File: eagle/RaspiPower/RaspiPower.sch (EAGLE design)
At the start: 26 parts, among them J5 AVR_SPI_PROG_3X2PTH, K1 4052

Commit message: Last changes before routing, added power LED
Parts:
- added J10: (no value), SparkFun-Connectors:CONN_01PTH_NO_SILK_YES_STOP
- added JOUT: (no value), SparkFun-Connectors:CONN_02LOCK_LONGPADS
- added LED_POWER2: (no value), SparkFun-LED:LED-FKIT-1206
- added R6: 1k, resistor:R-EU_R1206W
- D1: device diode:DIODE-D-2.5 -> diode:DIODE-D-5
- J6: device SparkFun-Connectors:CONN_02LOCK_LONGPADS -> SparkFun-Connectors:CONN_01PTH_NO_SILK_YES_STOP
- R4, R5: value 1k -> 10k
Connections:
- new net N$1: LED_POWER2.A, R6.1
- net GND: now also JOUT.2, LED_POWER2.C; no longer J6.2
- net N$3: now also JOUT.1; no longer J6.1
- net VCC: now also R6.2
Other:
- note added: "No resistor: - 97ohm in the relay coil for 942H-2C-5DS - 131ohm in the relay coil for HK4100F"
- note removed: "No resistor (97ohm in the relay coil)"
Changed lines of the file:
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@@
 <part name="K1" library="relay" deviceset="4052" device=""/>
 <part name="R3" library="resistor" deviceset="R-EU_" device="0204/7" value="1k"/>
-<part name="D1" library="diode" deviceset="DIODE-" device="D-2.5"/>
+<part name="D1" library="diode" deviceset="DIODE-" device="D-5"/>
 <part name="JP3" library="SparkFun-Jumpers" deviceset="JUMPER-SMT_3_NO" device="_SILK" value=""/>
 <part name="NPNOR1" library="transistor" deviceset="*-NPN-" device="TO92-ECB" value="2SC2120"/>
@@
 <part name="R1" library="resistor" deviceset="R-EU_" device="0207/2V" value="1k"/>
 <part name="R2" library="resistor" deviceset="R-EU_" device="0207/2V" value="1k"/>
-<part name="R4" library="resistor" deviceset="R-EU_" device="0207/2V" value="1k"/>
+<part name="R4" library="resistor" deviceset="R-EU_" device="0207/2V" value="10k"/>
 <part name="JP1" library="SparkFun-Jumpers" deviceset="JUMPER-SMT_3_NO" device="_SILK" value=""/>
 <part name="SUPPLY3" library="SparkFun-PowerSymbols" deviceset="VCC" device=""/>
-<part name="R5" library="resistor" deviceset="R-EU_" device="0207/2V" value="1k"/>
+<part name="R5" library="resistor" deviceset="R-EU_" device="0207/2V" value="10k"/>
 <part name="J2" library="SparkFun-Connectors" deviceset="CONN_05X2" device="PTH"/>
 <part name="J5" library="SparkFun-Connectors" deviceset="AVR_SPI_PROG_3X2" device="PTH"/>
 <part name="U$2" library="huike" deviceset="HK410?F-*" device="0" technology="DC5V"/>
-<part name="J6" library="SparkFun-Connectors" deviceset="CONN_02" device="LOCK_LONGPADS"/>
+<part name="JOUT" library="SparkFun-Connectors" deviceset="CONN_02" device="LOCK_LONGPADS"/>
 <part name="J1" library="SparkFun-Connectors" deviceset="CONN_02" device="LOCK_LONGPADS"/>
 <part name="J7" library="SparkFun-Connectors" deviceset="CONN_05X2" device="PTH"/>
 <part name="J8" library="SparkFun-Connectors" deviceset="CONN_05X2" device="PTH"/>
 <part name="J9" library="SparkFun-Connectors" deviceset="CONN_01" device="PTH_NO_SILK_YES_STOP"/>
+<part name="GND4" library="SparkFun-PowerSymbols" deviceset="GND" device=""/>
+<part name="R6" library="resistor" deviceset="R-EU_" device="R1206W" value="1k"/>
+<part name="LED_POWER2" library="SparkFun-LED" deviceset="LED" device="-FKIT-1206"/>
+<part name="SUPPLY4" library="SparkFun-PowerSymbols" deviceset="VCC" device=""/>
+<part name="GND5" library="SparkFun-PowerSymbols" deviceset="GND" device=""/>
+<part name="J6" library="SparkFun-Connectors" deviceset="CONN_01" device="PTH_NO_SILK_YES_STOP"/>
+<part name="J10" library="SparkFun-Connectors" deviceset="CONN_01" device="PTH_NO_SILK_YES_STOP"/>
 </parts>
 <sheets>
 <sheet>
 <plain>
-<text x="88.9" y="-17.78" size="1.778" layer="91">No resistor (97ohm in the relay coil)</text>
+<text x="88.9" y="5.08" size="1.778" layer="97">No resistor:
+- 97ohm in the relay coil for 942H-2C-5DS
+- 131ohm in the relay coil for HK4100F</text>
 </plain>
 <instances>
@@
 <instance part="U$2" gate="G$1" x="99.06" y="-12.7"/>
 <instance part="U$2" gate="G$2" x="132.08" y="-12.7"/>
-<instance part="J6" gate="G$1" x="144.78" y="-33.02" rot="R180"/>
+<instance part="JOUT" gate="G$1" x="144.78" y="-33.02" rot="R180"/>
 <instance part="J1" gate="G$1" x="-15.24" y="129.54"/>
 <instance part="J7" gate="G$1" x="134.62" y="101.6"/>
 <instance part="J8" gate="G$1" x="134.62" y="119.38"/>
 <instance part="J9" gate="G$1" x="149.86" y="-12.7" rot="R90"/>
+<instance part="GND4" gate="1" x="86.36" y="-45.72"/>
+<instance part="R6" gate="G$1" x="25.4" y="-7.62" rot="R90"/>
+<instance part="LED_POWER2" gate="G$1" x="33.02" y="-17.78"/>
+<instance part="SUPPLY4" gate="G$1" x="25.4" y="0"/>
+<instance part="GND5" gate="1" x="25.4" y="-30.48"/>
+<instance part="J6" gate="G$1" x="152.4" y="-35.56" rot="R90"/>
+<instance part="J10" gate="G$1" x="157.48" y="-35.56" rot="R90"/>
 </instances>
 <busses>
@@
 <wire x1="101.6" y1="152.4" x2="109.22" y2="152.4" width="0.1524" layer="91"/>
 <label x="104.14" y="152.4" size="1.778" layer="95"/>
+</segment>
+<segment>
+<pinref part="R6" gate="G$1" pin="2"/>
+<pinref part="SUPPLY4" gate="G$1" pin="VCC"/>
+<wire x1="25.4" y1="0" x2="25.4" y2="-2.54" width="0.1524" layer="91"/>
 </segment>
 </net>
@@
 <wire x1="91.44" y1="-38.1" x2="91.44" y2="-40.64" width="0.1524" layer="91"/>
 <wire x1="91.44" y1="-40.64" x2="86.36" y2="-40.64" width="0.1524" layer="91"/>
-<pinref part="J6" gate="G$1" pin="2"/>
+<pinref part="JOUT" gate="G$1" pin="2"/>
 <wire x1="137.16" y1="-35.56" x2="116.84" y2="-35.56" width="0.1524" layer="91"/>
 <wire x1="116.84" y1="-35.56" x2="116.84" y2="-38.1" width="0.1524" layer="91"/>
+<pinref part="GND4" gate="1" pin="GND"/>
 </segment>
 <segment>
@@
 <wire x1="101.6" y1="147.32" x2="109.22" y2="147.32" width="0.1524" layer="91"/>
 <label x="104.14" y="147.32" size="1.778" layer="95"/>
+</segment>
+<segment>
+<pinref part="GND5" gate="1" pin="GND"/>
+<wire x1="25.4" y1="-27.94" x2="25.4" y2="-22.86" width="0.1524" layer="91"/>
+<pinref part="LED_POWER2" gate="G$1" pin="C"/>
+<wire x1="25.4" y1="-22.86" x2="33.02" y2="-22.86" width="0.1524" layer="91"/>
 </segment>
 </net>
@@
 <pinref part="U$2" gate="G$2" pin="P"/>
 <wire x1="132.08" y1="-15.24" x2="116.84" y2="-15.24" width="0.1524" layer="91"/>
-<pinref part="J6" gate="G$1" pin="1"/>
+<pinref part="JOUT" gate="G$1" pin="1"/>
 <wire x1="116.84" y1="-30.48" x2="137.16" y2="-30.48" width="0.1524" layer="91"/>
 <wire x1="137.16" y1="-30.48" x2="137.16" y2="-33.02" width="0.1524" layer="91"/>
@@
 <label x="99.06" y="81.28" size="1.778" layer="95"/>
 <pinref part="J2" gate="G$1" pin="7"/>
+<junction x="63.5" y="86.36"/>
+</segment>
+</net>
+<net name="N$1" class="0">
+<segment>
+<pinref part="LED_POWER2" gate="G$1" pin="A"/>
+<pinref part="R6" gate="G$1" pin="1"/>
+<wire x1="33.02" y1="-15.24" x2="25.4" y2="-15.24" width="0.1524" layer="91"/>
+<wire x1="25.4" y1="-12.7" x2="25.4" y2="-15.24" width="0.1524" layer="91"/>
 </segment>
 </net>
@@
 </schematic>
 </drawing>
+<compatibility>
+<note version="6.3" minversion="6.2.2" severity="warning">
+Since Version 6.2.2 text objects can contain more than one line,
+which will not be processed correctly with this version.
+</note>
+</compatibility>
 </eagle>

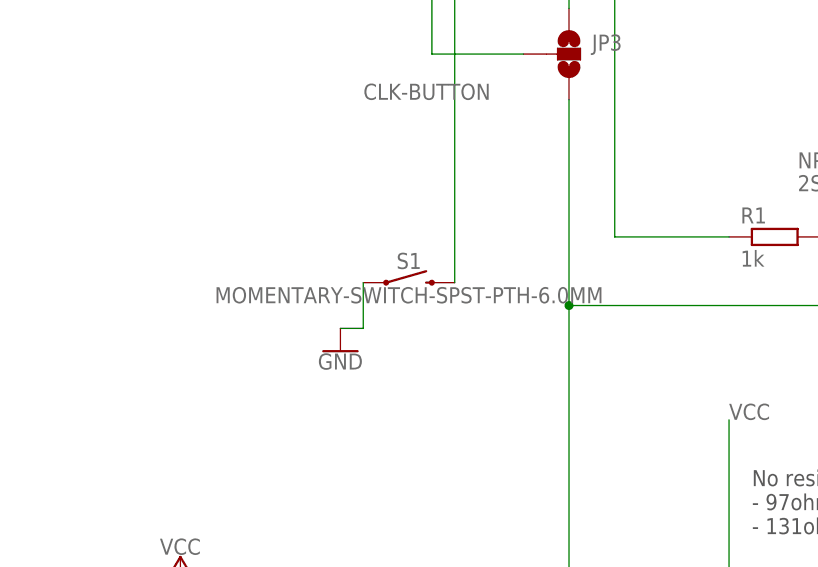
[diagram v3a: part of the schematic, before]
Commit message: switched pins of tact switch for easier routing
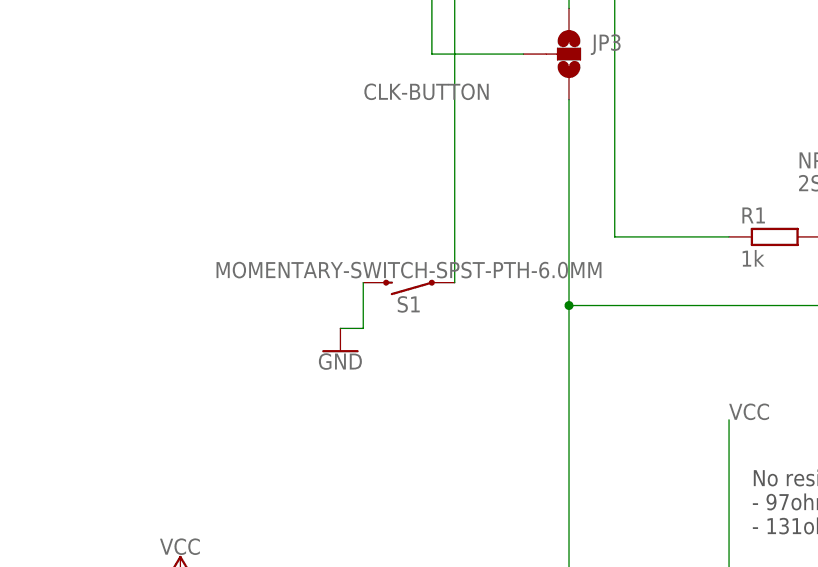
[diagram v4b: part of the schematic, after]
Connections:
- net CLK-BUTTON: now also S1.1; no longer S1.2
- net GND: now also S1.2; no longer S1.1
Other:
- moved on the sheet: S1
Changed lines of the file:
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@@
 <part name="J3" library="SparkFun-Connectors" deviceset="CONN_03" device=""/>
 <part name="J4" library="SparkFun-Connectors" deviceset="CONN_03" device=""/>
-<part name="S1" library="SparkFun-Switches" deviceset="MOMENTARY-SWITCH-SPST" device="-PTH-6.0MM"/>
 <part name="GND2" library="SparkFun-PowerSymbols" deviceset="GND" device=""/>
 <part name="NRELAY" library="transistor" deviceset="*-NPN-" device="TO92-ECB" value="2SC2120"/>
@@
 <part name="J6" library="SparkFun-Connectors" deviceset="CONN_01" device="PTH_NO_SILK_YES_STOP"/>
 <part name="J10" library="SparkFun-Connectors" deviceset="CONN_01" device="PTH_NO_SILK_YES_STOP"/>
+<part name="S1" library="SparkFun-Switches" deviceset="MOMENTARY-SWITCH-SPST" device="-PTH-6.0MM"/>
 </parts>
 <sheets>
@@
 <instance part="J3" gate="J$1" x="71.12" y="83.82" rot="R180"/>
 <instance part="J4" gate="J$1" x="5.08" y="83.82"/>
-<instance part="S1" gate="G$1" x="50.8" y="33.02"/>
 <instance part="GND2" gate="1" x="43.18" y="25.4"/>
 <instance part="NRELAY" gate="G$1" x="83.82" y="-35.56"/>
@@
 <instance part="J6" gate="G$1" x="152.4" y="-35.56" rot="R90"/>
 <instance part="J10" gate="G$1" x="157.48" y="-35.56" rot="R90"/>
+<instance part="S1" gate="G$1" x="50.8" y="33.02" rot="R180"/>
 </instances>
 <busses>
@@
 <segment>
 <pinref part="GND2" gate="1" pin="GND"/>
-<pinref part="S1" gate="G$1" pin="1"/>
 <wire x1="43.18" y1="27.94" x2="45.72" y2="27.94" width="0.1524" layer="91"/>
 <wire x1="45.72" y1="27.94" x2="45.72" y2="33.02" width="0.1524" layer="91"/>
+<pinref part="S1" gate="G$1" pin="2"/>
 </segment>
 <segment>
@@
 <pinref part="J3" gate="J$1" pin="3"/>
 <wire x1="55.88" y1="81.28" x2="63.5" y2="81.28" width="0.1524" layer="91"/>
-<pinref part="S1" gate="G$1" pin="2"/>
+<label x="45.72" y="53.34" size="1.778" layer="95"/>
 <wire x1="55.88" y1="33.02" x2="55.88" y2="81.28" width="0.1524" layer="91"/>
 <junction x="55.88" y="81.28"/>
-<label x="45.72" y="53.34" size="1.778" layer="95"/>
-</segment>
-<segment>
+<pinref part="S1" gate="G$1" pin="1"/>
+</segment>
+<segment>

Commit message: Few changes, board in version 1.0 for prod
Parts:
- added C1: 10uF, resistor:CPOL-EUE2.5-5
- renumbered J1 to JIN, J5 to JSPIPROG
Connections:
- removed net N$10: JP1.2, R5.1
- new net N$7: JP1.1, R5.1
- net GND: now also C1.-
- net PI_IS_ON: now also JP1.3; no longer JP1.1
- net RESET: now also JP1.2; no longer JP1.3
- net VCC: now also C1.+
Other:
- note added: "JP1-A"
- note added: "JP1-B"
- note added: "JP3-A"
- note added: "JP3-B"
- moved on the sheet: JP1
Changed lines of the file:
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@@
 <part name="R5" library="resistor" deviceset="R-EU_" device="0207/2V" value="10k"/>
 <part name="J2" library="SparkFun-Connectors" deviceset="CONN_05X2" device="PTH"/>
-<part name="J5" library="SparkFun-Connectors" deviceset="AVR_SPI_PROG_3X2" device="PTH"/>
+<part name="JSPIPROG" library="SparkFun-Connectors" deviceset="AVR_SPI_PROG_3X2" device="PTH"/>
 <part name="U$2" library="huike" deviceset="HK410?F-*" device="0" technology="DC5V"/>
 <part name="JOUT" library="SparkFun-Connectors" deviceset="CONN_02" device="LOCK_LONGPADS"/>
-<part name="J1" library="SparkFun-Connectors" deviceset="CONN_02" device="LOCK_LONGPADS"/>
+<part name="JIN" library="SparkFun-Connectors" deviceset="CONN_02" device="LOCK_LONGPADS"/>
 <part name="J7" library="SparkFun-Connectors" deviceset="CONN_05X2" device="PTH"/>
 <part name="J8" library="SparkFun-Connectors" deviceset="CONN_05X2" device="PTH"/>
@@
 <part name="J10" library="SparkFun-Connectors" deviceset="CONN_01" device="PTH_NO_SILK_YES_STOP"/>
 <part name="S1" library="SparkFun-Switches" deviceset="MOMENTARY-SWITCH-SPST" device="-PTH-6.0MM"/>
+<part name="C1" library="resistor" deviceset="CPOL-EU" device="E2.5-5" value="10uF"/>
 </parts>
 <sheets>
@@
 - 97ohm in the relay coil for 942H-2C-5DS
 - 131ohm in the relay coil for HK4100F</text>
+<wire x1="91.44" y1="106.68" x2="96.52" y2="106.68" width="0.1524" layer="97"/>
+<wire x1="96.52" y1="106.68" x2="96.52" y2="109.22" width="0.1524" layer="97"/>
+<wire x1="60.96" y1="55.88" x2="66.04" y2="55.88" width="0.1524" layer="97"/>
+<wire x1="66.04" y1="55.88" x2="66.04" y2="50.8" width="0.1524" layer="97"/>
+<wire x1="60.96" y1="60.96" x2="66.04" y2="60.96" width="0.1524" layer="97"/>
+<wire x1="66.04" y1="60.96" x2="66.04" y2="66.04" width="0.1524" layer="97"/>
+<text x="64.77" y="61.722" size="1.778" layer="97" rot="R90">JP3-A</text>
+<text x="65.278" y="48.006" size="1.778" layer="97" rot="R90">JP3-B</text>
+<text x="88.646" y="107.696" size="1.778" layer="97">JP1-A</text>
+<text x="88.9" y="99.06" size="1.778" layer="97">JP1-B</text>
+<wire x1="91.44" y1="101.6" x2="96.52" y2="101.6" width="0.1524" layer="97"/>
+<wire x1="96.52" y1="101.6" x2="96.52" y2="99.06" width="0.1524" layer="97"/>
 </plain>
 <instances>
@@
 <instance part="R2" gate="G$1" x="109.22" y="50.8"/>
 <instance part="R4" gate="G$1" x="129.54" y="25.4" rot="R90"/>
-<instance part="JP1" gate="G$1" x="99.06" y="104.14" rot="R270"/>
+<instance part="JP1" gate="G$1" x="99.06" y="104.14"/>
 <instance part="SUPPLY3" gate="G$1" x="99.06" y="121.92"/>
 <instance part="R5" gate="G$1" x="99.06" y="116.84" rot="R90"/>
 <instance part="J2" gate="G$1" x="134.62" y="83.82"/>
-<instance part="J5" gate="G$1" x="91.44" y="149.86"/>
+<instance part="JSPIPROG" gate="G$1" x="91.44" y="149.86"/>
 <instance part="U$2" gate="G$1" x="99.06" y="-12.7"/>
 <instance part="U$2" gate="G$2" x="132.08" y="-12.7"/>
 <instance part="JOUT" gate="G$1" x="144.78" y="-33.02" rot="R180"/>
-<instance part="J1" gate="G$1" x="-15.24" y="129.54"/>
+<instance part="JIN" gate="G$1" x="-15.24" y="129.54"/>
 <instance part="J7" gate="G$1" x="134.62" y="101.6"/>
 <instance part="J8" gate="G$1" x="134.62" y="119.38"/>
@@
 <instance part="J10" gate="G$1" x="157.48" y="-35.56" rot="R90"/>
 <instance part="S1" gate="G$1" x="50.8" y="33.02" rot="R180"/>
+<instance part="C1" gate="G$1" x="-27.94" y="132.08"/>
 </instances>
 <busses>
@@
 <wire x1="2.54" y1="137.16" x2="2.54" y2="147.32" width="0.1524" layer="91"/>
 <pinref part="SUPPLY1" gate="G$1" pin="VCC"/>
-<pinref part="J1" gate="G$1" pin="2"/>
+<pinref part="JIN" gate="G$1" pin="2"/>
 <wire x1="2.54" y1="137.16" x2="-7.62" y2="137.16" width="0.1524" layer="91"/>
 <wire x1="-7.62" y1="137.16" x2="-7.62" y2="132.08" width="0.1524" layer="91"/>
+<pinref part="C1" gate="G$1" pin="+"/>
+<wire x1="-7.62" y1="137.16" x2="-27.94" y2="137.16" width="0.1524" layer="91"/>
+<wire x1="-27.94" y1="137.16" x2="-27.94" y2="134.62" width="0.1524" layer="91"/>
 </segment>
 <segment>
@@
 </segment>
 <segment>
-<pinref part="J5" gate="G$1" pin="2"/>
+<pinref part="JSPIPROG" gate="G$1" pin="2"/>
 <wire x1="101.6" y1="152.4" x2="109.22" y2="152.4" width="0.1524" layer="91"/>
 <label x="104.14" y="152.4" size="1.778" layer="95"/>
@@
 <junction x="25.4" y="127"/>
 <pinref part="GND1" gate="1" pin="GND"/>
-<pinref part="J1" gate="G$1" pin="1"/>
+<pinref part="JIN" gate="G$1" pin="1"/>
 <wire x1="2.54" y1="127" x2="-7.62" y2="127" width="0.1524" layer="91"/>
 <wire x1="-7.62" y1="127" x2="-7.62" y2="129.54" width="0.1524" layer="91"/>
+<pinref part="C1" gate="G$1" pin="-"/>
+<wire x1="-7.62" y1="127" x2="-27.94" y2="127" width="0.1524" layer="91"/>
 </segment>
 <segment>
@@
 </segment>
 <segment>
-<pinref part="J5" gate="G$1" pin="6"/>
+<pinref part="JSPIPROG" gate="G$1" pin="6"/>
 <wire x1="101.6" y1="147.32" x2="109.22" y2="147.32" width="0.1524" layer="91"/>
 <label x="104.14" y="147.32" size="1.778" layer="95"/>
@@
 </segment>
 <segment>
-<pinref part="J5" gate="G$1" pin="3"/>
+<pinref part="JSPIPROG" gate="G$1" pin="3"/>
 <wire x1="83.82" y1="149.86" x2="60.96" y2="149.86" width="0.1524" layer="91"/>
 <label x="60.96" y="149.86" size="1.778" layer="95"/>
@@
 <pinref part="J4" gate="J$1" pin="1"/>
 <wire x1="17.78" y1="81.28" x2="12.7" y2="81.28" width="0.1524" layer="91"/>
-<wire x1="93.98" y1="104.14" x2="22.86" y2="104.14" width="0.1524" layer="91"/>
 <wire x1="22.86" y1="104.14" x2="22.86" y2="88.9" width="0.1524" layer="91"/>
-<pinref part="JP1" gate="G$1" pin="3"/>
-</segment>
-<segment>
-<pinref part="J5" gate="G$1" pin="5"/>
+<pinref part="JP1" gate="G$1" pin="2"/>
+<wire x1="22.86" y1="104.14" x2="93.98" y2="104.14" width="0.1524" layer="91"/>
+</segment>
+<segment>
+<pinref part="JSPIPROG" gate="G$1" pin="5"/>
 <wire x1="83.82" y1="147.32" x2="60.96" y2="147.32" width="0.1524" layer="91"/>
 <label x="60.96" y="147.32" size="1.778" layer="95"/>
@@
 <wire x1="127" y1="86.36" x2="106.68" y2="86.36" width="0.1524" layer="91"/>
 <wire x1="106.68" y1="86.36" x2="106.68" y2="99.06" width="0.1524" layer="91"/>
-<wire x1="106.68" y1="99.06" x2="104.14" y2="99.06" width="0.1524" layer="91"/>
-<wire x1="104.14" y1="99.06" x2="104.14" y2="104.14" width="0.1524" layer="91"/>
 <label x="106.68" y="86.36" size="1.778" layer="95"/>
 <pinref part="R2" gate="G$1" pin="1"/>
@@
 <wire x1="106.68" y1="76.2" x2="106.68" y2="86.36" width="0.1524" layer="91"/>
 <junction x="106.68" y="86.36"/>
-<pinref part="JP1" gate="G$1" pin="1"/>
 <pinref part="J2" gate="G$1" pin="3"/>
+<pinref part="JP1" gate="G$1" pin="3"/>
+<wire x1="99.06" y1="99.06" x2="106.68" y2="99.06" width="0.1524" layer="91"/>
 </segment>
 </net>
@@
 </segment>
 </net>
-<net name="N$10" class="0">
-<segment>
-<pinref part="R5" gate="G$1" pin="1"/>
-<pinref part="JP1" gate="G$1" pin="2"/>
-<wire x1="99.06" y1="111.76" x2="99.06" y2="109.22" width="0.1524" layer="91"/>
-</segment>
-</net>
 <net name="DATA-DOSHUTDN" class="0">
 <segment>
-<pinref part="J5" gate="G$1" pin="1"/>
+<pinref part="JSPIPROG" gate="G$1" pin="1"/>
 <wire x1="83.82" y1="152.4" x2="60.96" y2="152.4" width="0.1524" layer="91"/>
 <label x="60.96" y="152.4" size="1.778" layer="95"/>
@@
 <wire x1="63.5" y1="88.9" x2="63.5" y2="86.36" width="0.1524" layer="91"/>
 <wire x1="127" y1="81.28" x2="99.06" y2="81.28" width="0.1524" layer="91"/>
-<wire x1="99.06" y1="81.28" x2="99.06" y2="96.52" width="0.1524" layer="91"/>
-<wire x1="99.06" y1="96.52" x2="63.5" y2="96.52" width="0.1524" layer="91"/>
-<wire x1="63.5" y1="96.52" x2="63.5" y2="86.36" width="0.1524" layer="91"/>
+<wire x1="99.06" y1="81.28" x2="99.06" y2="91.44" width="0.1524" layer="91"/>
+<wire x1="99.06" y1="91.44" x2="63.5" y2="91.44" width="0.1524" layer="91"/>
+<wire x1="63.5" y1="91.44" x2="63.5" y2="86.36" width="0.1524" layer="91"/>
 <label x="99.06" y="81.28" size="1.778" layer="95"/>
 <pinref part="J2" gate="G$1" pin="7"/>
@@
 </segment>
 </net>
+<net name="N$7" class="0">
+<segment>
+<pinref part="JP1" gate="G$1" pin="1"/>
+<pinref part="R5" gate="G$1" pin="1"/>
+<wire x1="99.06" y1="109.22" x2="99.06" y2="111.76" width="0.1524" layer="91"/>
+</segment>
+</net>

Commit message: Still fixing the board, not finished
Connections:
- net VCC: now also K12.S, U$2G$2.S; no longer K12.O, U$2G$2.O
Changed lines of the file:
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@@
 <pinref part="K1" gate="1" pin="1"/>
 <pinref part="D1" gate="G$1" pin="C"/>
-<pinref part="K1" gate="2" pin="O"/>
-<wire x1="86.36" y1="0" x2="121.92" y2="0" width="0.1524" layer="91"/>
-<wire x1="121.92" y1="0" x2="121.92" y2="-7.62" width="0.1524" layer="91"/>
-<pinref part="U$2" gate="G$2" pin="O"/>
-<wire x1="121.92" y1="0" x2="137.16" y2="0" width="0.1524" layer="91"/>
-<wire x1="137.16" y1="0" x2="137.16" y2="-7.62" width="0.1524" layer="91"/>
+<wire x1="86.36" y1="0" x2="111.76" y2="0" width="0.1524" layer="91"/>
 <pinref part="U$2" gate="G$1" pin="+"/>
+<wire x1="111.76" y1="0" x2="127" y2="0" width="0.1524" layer="91"/>
 <wire x1="86.36" y1="-7.62" x2="99.06" y2="-7.62" width="0.1524" layer="91"/>
+<pinref part="K1" gate="2" pin="S"/>
+<wire x1="111.76" y1="-7.62" x2="111.76" y2="0" width="0.1524" layer="91"/>
+<junction x="111.76" y="0"/>
+<pinref part="U$2" gate="G$2" pin="S"/>
+<wire x1="127" y1="0" x2="127" y2="-7.62" width="0.1524" layer="91"/>
 </segment>
 <segment>
